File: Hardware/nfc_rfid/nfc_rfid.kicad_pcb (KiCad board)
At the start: 4 copper layers, 74.1 x 32 mm, 158 parts, among them IC1 ST25R3916-AQWT, IC2 FAN48610UC50X, J1 BW0033AG-L3.4W0.9H1.8, J2 BW0033AG-L3.4W0.9H1.8, J3 HC-FPC-05-09-18RLTAG, J4 +, J5 -, J6 AFH34-S06FIA-1H, J7 BW0033AG-L3.4W0.9H1.8, J8 BW0033AG-L3.4W0.9H1.8, Q1 AO3400A, Q2 DMN2004TK-7, Q3 DMP2004TK-7, Q4 DMN2004TK-7, Q5 DMN5L06TK-7, U1 LMV358AIDGKR, U2 LMV331IDCKR, U3 LMV358AIDGKR, Y1 CF4027M12010001

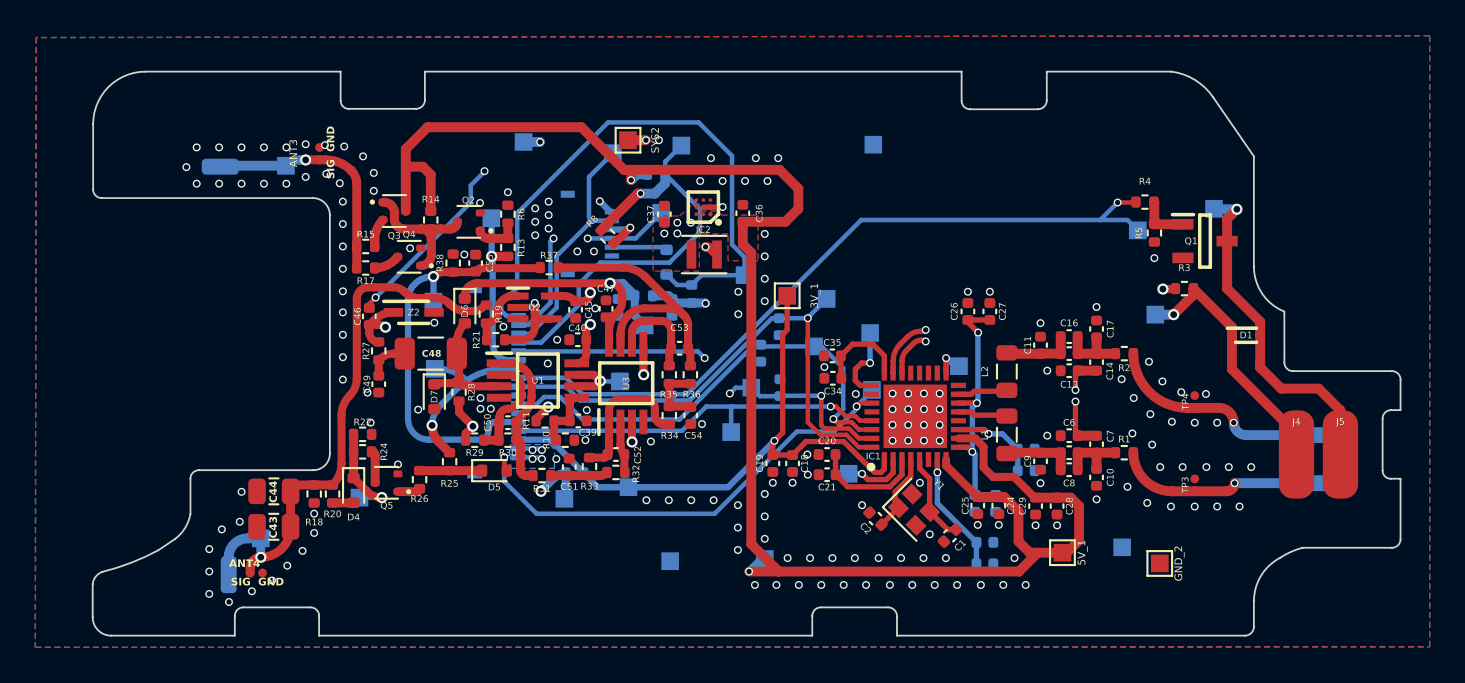
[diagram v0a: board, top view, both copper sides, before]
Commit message: PCB: nfc_rfid: add more stitching vias silkscreen: add more silkscreens
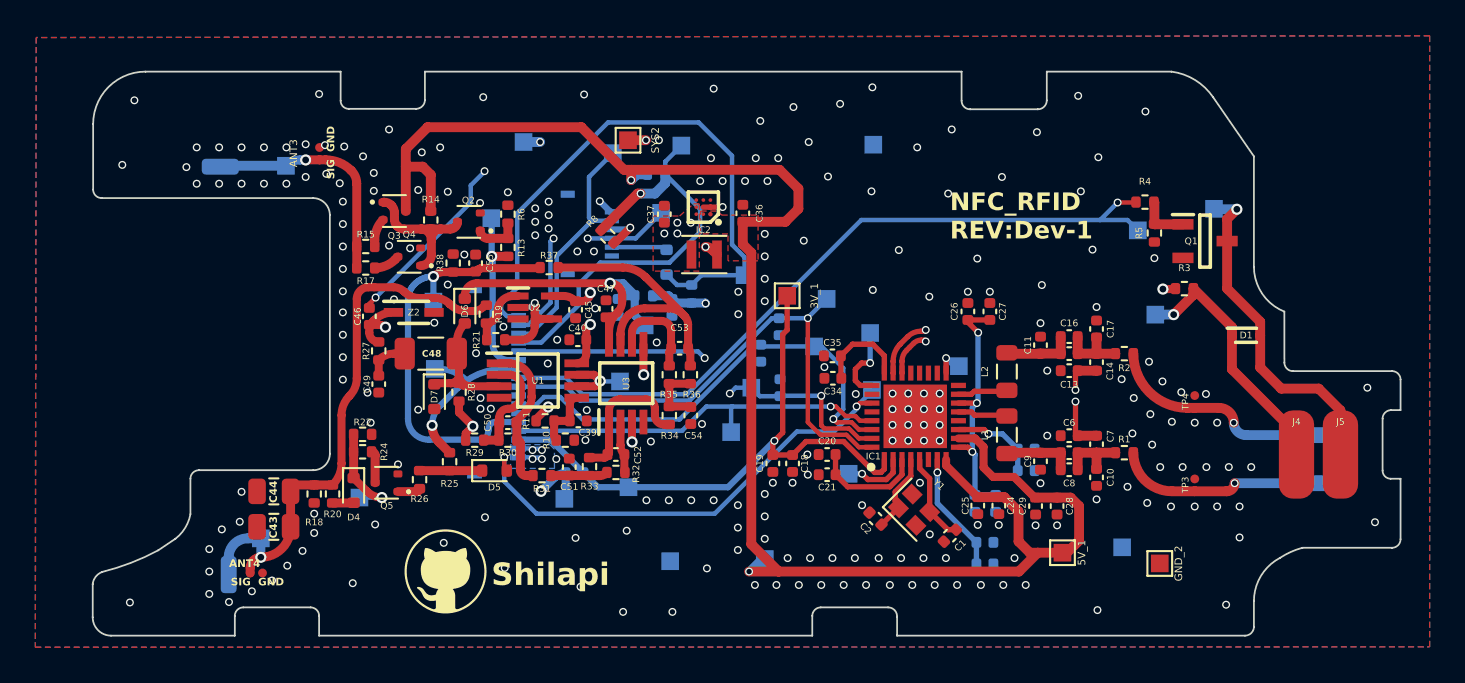
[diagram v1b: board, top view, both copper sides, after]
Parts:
- added G***: LOGO, Library:GITHUB LOGO, F.Cu at (91.6, 75.9)
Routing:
- net GND: vias 178 -> 234
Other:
- board text added: "NFC_RFID REV:Dev-1"
- board text added: "Shilapi"
